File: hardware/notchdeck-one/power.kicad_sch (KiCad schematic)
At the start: 21 parts, among them J1 USB-C, J2 BAT 1S, Q1 AO3401A, U2 AP2112K-3.3, U3 MCP73831-2-OT, U4 MAX17048, U7 USBLC6-2SC6, U8 74LVC1G125

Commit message: Add schematic wiring notes support
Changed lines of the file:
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@@
 		(instances
 			(project "notchdeck-one"
-				(path "/9b1c0f7a-1d2e-4a3b-8c5d-0e6f7a8b9c01/7d2dd40e-5097-4a0f-9306-a516a342b95f"
+				(path "/9b1c0f7a-1d2e-4a3b-8c5d-0e6f7a8b9c01/2c77e6d8-3afb-4a5f-bda1-2cf5540b755c"
 					(reference "J1")
 					(unit 1)
@@
 		(instances
 			(project "notchdeck-one"
-				(path "/9b1c0f7a-1d2e-4a3b-8c5d-0e6f7a8b9c01/7d2dd40e-5097-4a0f-9306-a516a342b95f"
+				(path "/9b1c0f7a-1d2e-4a3b-8c5d-0e6f7a8b9c01/2c77e6d8-3afb-4a5f-bda1-2cf5540b755c"
 					(reference "U7")
 					(unit 1)
@@
 		(instances
 			(project "notchdeck-one"
-				(path "/9b1c0f7a-1d2e-4a3b-8c5d-0e6f7a8b9c01/7d2dd40e-5097-4a0f-9306-a516a342b95f"
+				(path "/9b1c0f7a-1d2e-4a3b-8c5d-0e6f7a8b9c01/2c77e6d8-3afb-4a5f-bda1-2cf5540b755c"
 					(reference "R1")
 					(unit 1)
@@
 		(instances
 			(project "notchdeck-one"
-				(path "/9b1c0f7a-1d2e-4a3b-8c5d-0e6f7a8b9c01/7d2dd40e-5097-4a0f-9306-a516a342b95f"
+				(path "/9b1c0f7a-1d2e-4a3b-8c5d-0e6f7a8b9c01/2c77e6d8-3afb-4a5f-bda1-2cf5540b755c"
 					(reference "R2")
 					(unit 1)
@@
 		(instances
 			(project "notchdeck-one"
-				(path "/9b1c0f7a-1d2e-4a3b-8c5d-0e6f7a8b9c01/7d2dd40e-5097-4a0f-9306-a516a342b95f"
+				(path "/9b1c0f7a-1d2e-4a3b-8c5d-0e6f7a8b9c01/2c77e6d8-3afb-4a5f-bda1-2cf5540b755c"
 					(reference "U3")
 					(unit 1)
@@
 		(instances
 			(project "notchdeck-one"
-				(path "/9b1c0f7a-1d2e-4a3b-8c5d-0e6f7a8b9c01/7d2dd40e-5097-4a0f-9306-a516a342b95f"
+				(path "/9b1c0f7a-1d2e-4a3b-8c5d-0e6f7a8b9c01/2c77e6d8-3afb-4a5f-bda1-2cf5540b755c"
 					(reference "R3")
 					(unit 1)
@@
 		(instances
 			(project "notchdeck-one"
-				(path "/9b1c0f7a-1d2e-4a3b-8c5d-0e6f7a8b9c01/7d2dd40e-5097-4a0f-9306-a516a342b95f"
+				(path "/9b1c0f7a-1d2e-4a3b-8c5d-0e6f7a8b9c01/2c77e6d8-3afb-4a5f-bda1-2cf5540b755c"
 					(reference "U2")
 					(unit 1)
@@
 		(instances
 			(project "notchdeck-one"
-				(path "/9b1c0f7a-1d2e-4a3b-8c5d-0e6f7a8b9c01/7d2dd40e-5097-4a0f-9306-a516a342b95f"
+				(path "/9b1c0f7a-1d2e-4a3b-8c5d-0e6f7a8b9c01/2c77e6d8-3afb-4a5f-bda1-2cf5540b755c"
 					(reference "C7")
 					(unit 1)
@@
 		(instances
 			(project "notchdeck-one"
-				(path "/9b1c0f7a-1d2e-4a3b-8c5d-0e6f7a8b9c01/7d2dd40e-5097-4a0f-9306-a516a342b95f"
+				(path "/9b1c0f7a-1d2e-4a3b-8c5d-0e6f7a8b9c01/2c77e6d8-3afb-4a5f-bda1-2cf5540b755c"
 					(reference "C8")
 					(unit 1)
@@
 		(instances
 			(project "notchdeck-one"
-				(path "/9b1c0f7a-1d2e-4a3b-8c5d-0e6f7a8b9c01/7d2dd40e-5097-4a0f-9306-a516a342b95f"
+				(path "/9b1c0f7a-1d2e-4a3b-8c5d-0e6f7a8b9c01/2c77e6d8-3afb-4a5f-bda1-2cf5540b755c"
 					(reference "C9")
 					(unit 1)
@@
 		(instances
 			(project "notchdeck-one"
-				(path "/9b1c0f7a-1d2e-4a3b-8c5d-0e6f7a8b9c01/7d2dd40e-5097-4a0f-9306-a516a342b95f"
+				(path "/9b1c0f7a-1d2e-4a3b-8c5d-0e6f7a8b9c01/2c77e6d8-3afb-4a5f-bda1-2cf5540b755c"
 					(reference "Q1")
 					(unit 1)
@@
 		(instances
 			(project "notchdeck-one"
-				(path "/9b1c0f7a-1d2e-4a3b-8c5d-0e6f7a8b9c01/7d2dd40e-5097-4a0f-9306-a516a342b95f"
+				(path "/9b1c0f7a-1d2e-4a3b-8c5d-0e6f7a8b9c01/2c77e6d8-3afb-4a5f-bda1-2cf5540b755c"
 					(reference "D_PP")
 					(unit 1)
@@
 		(instances
 			(project "notchdeck-one"
-				(path "/9b1c0f7a-1d2e-4a3b-8c5d-0e6f7a8b9c01/7d2dd40e-5097-4a0f-9306-a516a342b95f"
+				(path "/9b1c0f7a-1d2e-4a3b-8c5d-0e6f7a8b9c01/2c77e6d8-3afb-4a5f-bda1-2cf5540b755c"
 					(reference "R4")
 					(unit 1)
@@
 		(instances
 			(project "notchdeck-one"
-				(path "/9b1c0f7a-1d2e-4a3b-8c5d-0e6f7a8b9c01/7d2dd40e-5097-4a0f-9306-a516a342b95f"
+				(path "/9b1c0f7a-1d2e-4a3b-8c5d-0e6f7a8b9c01/2c77e6d8-3afb-4a5f-bda1-2cf5540b755c"
 					(reference "R5")
 					(unit 1)
@@
 		(instances
 			(project "notchdeck-one"
-				(path "/9b1c0f7a-1d2e-4a3b-8c5d-0e6f7a8b9c01/7d2dd40e-5097-4a0f-9306-a516a342b95f"
+				(path "/9b1c0f7a-1d2e-4a3b-8c5d-0e6f7a8b9c01/2c77e6d8-3afb-4a5f-bda1-2cf5540b755c"
 					(reference "U4")
 					(unit 1)
@@
 		(instances
 			(project "notchdeck-one"
-				(path "/9b1c0f7a-1d2e-4a3b-8c5d-0e6f7a8b9c01/7d2dd40e-5097-4a0f-9306-a516a342b95f"
+				(path "/9b1c0f7a-1d2e-4a3b-8c5d-0e6f7a8b9c01/2c77e6d8-3afb-4a5f-bda1-2cf5540b755c"
 					(reference "C10")
 					(unit 1)
@@
 		(instances
 			(project "notchdeck-one"
-				(path "/9b1c0f7a-1d2e-4a3b-8c5d-0e6f7a8b9c01/7d2dd40e-5097-4a0f-9306-a516a342b95f"
+				(path "/9b1c0f7a-1d2e-4a3b-8c5d-0e6f7a8b9c01/2c77e6d8-3afb-4a5f-bda1-2cf5540b755c"
 					(reference "R6")
 					(unit 1)
@@
 		(instances
 			(project "notchdeck-one"
-				(path "/9b1c0f7a-1d2e-4a3b-8c5d-0e6f7a8b9c01/7d2dd40e-5097-4a0f-9306-a516a342b95f"
+				(path "/9b1c0f7a-1d2e-4a3b-8c5d-0e6f7a8b9c01/2c77e6d8-3afb-4a5f-bda1-2cf5540b755c"
 					(reference "R7")
 					(unit 1)
@@
 		(instances
 			(project "notchdeck-one"
-				(path "/9b1c0f7a-1d2e-4a3b-8c5d-0e6f7a8b9c01/7d2dd40e-5097-4a0f-9306-a516a342b95f"
+				(path "/9b1c0f7a-1d2e-4a3b-8c5d-0e6f7a8b9c01/2c77e6d8-3afb-4a5f-bda1-2cf5540b755c"
 					(reference "R8")
 					(unit 1)
@@
 		(instances
 			(project "notchdeck-one"
-				(path "/9b1c0f7a-1d2e-4a3b-8c5d-0e6f7a8b9c01/7d2dd40e-5097-4a0f-9306-a516a342b95f"
+				(path "/9b1c0f7a-1d2e-4a3b-8c5d-0e6f7a8b9c01/2c77e6d8-3afb-4a5f-bda1-2cf5540b755c"
 					(reference "J2")
 					(unit 1)
@@
 		(instances
 			(project "notchdeck-one"
-				(path "/9b1c0f7a-1d2e-4a3b-8c5d-0e6f7a8b9c01/7d2dd40e-5097-4a0f-9306-a516a342b95f"
+				(path "/9b1c0f7a-1d2e-4a3b-8c5d-0e6f7a8b9c01/2c77e6d8-3afb-4a5f-bda1-2cf5540b755c"
 					(reference "U8")
 					(unit 1)
@@
 		(exclude_from_sim no)
 		(at 15.00 175.00 0)
-		(effects (font (size 1.5 1.5)) (justify left top))
+		(effects (font (face "Courier New") (size 1.27 1.27)) (justify left top))
 	)
 	(sheet_instances

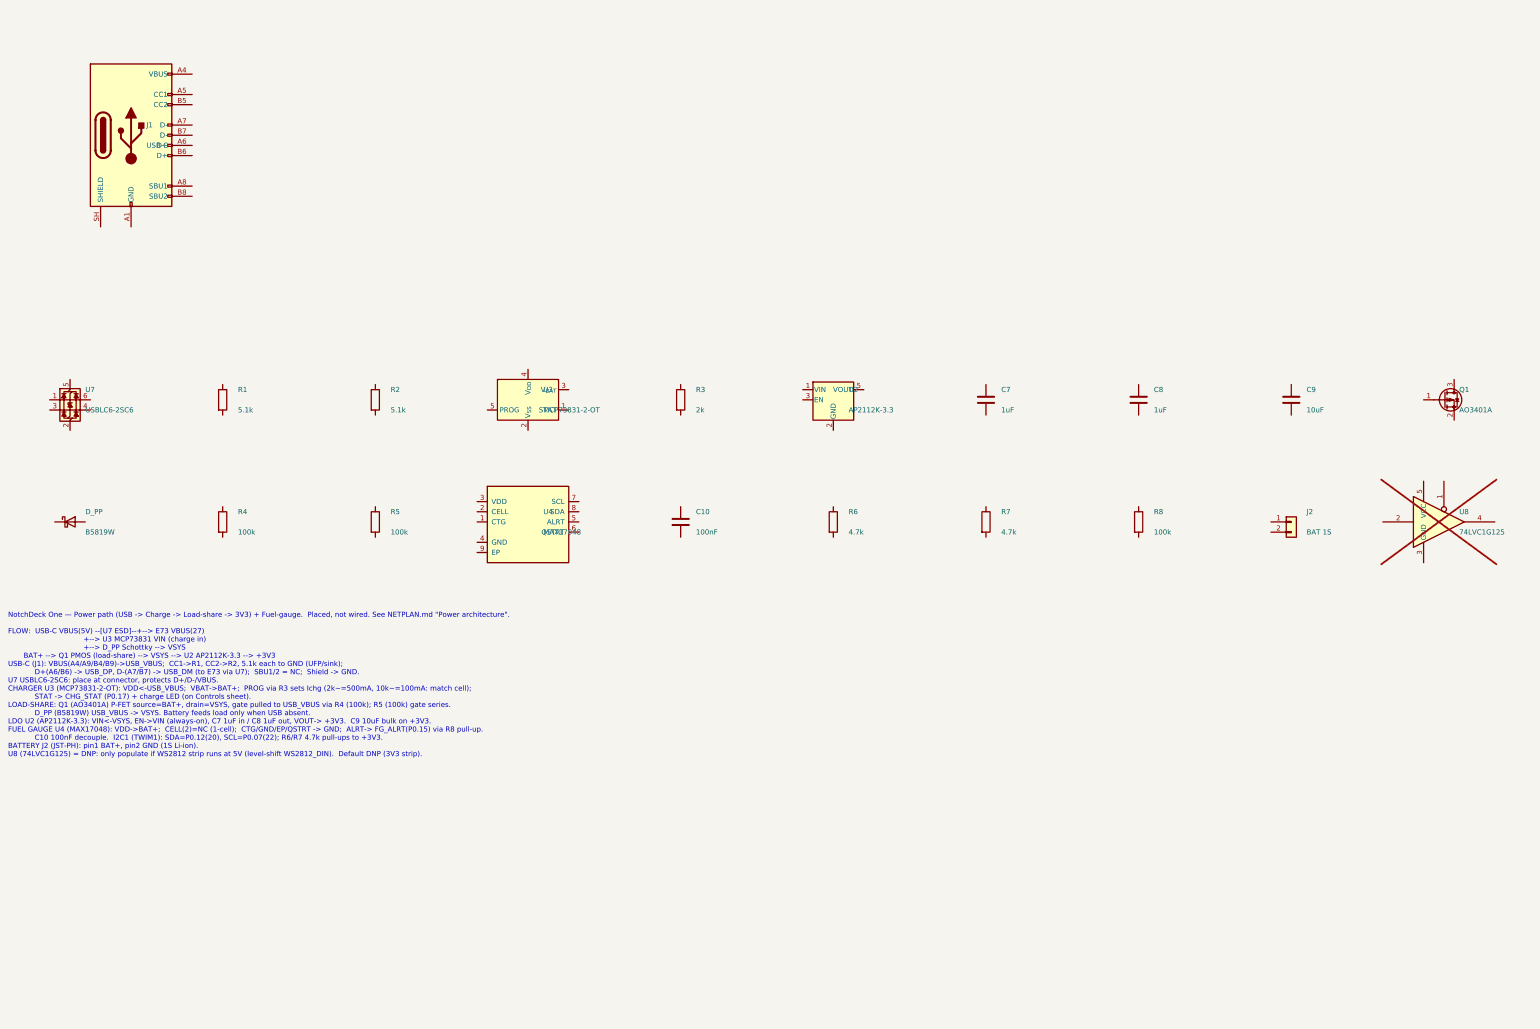
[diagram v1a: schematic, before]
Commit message: Wire and verify NotchDeck controller schematics
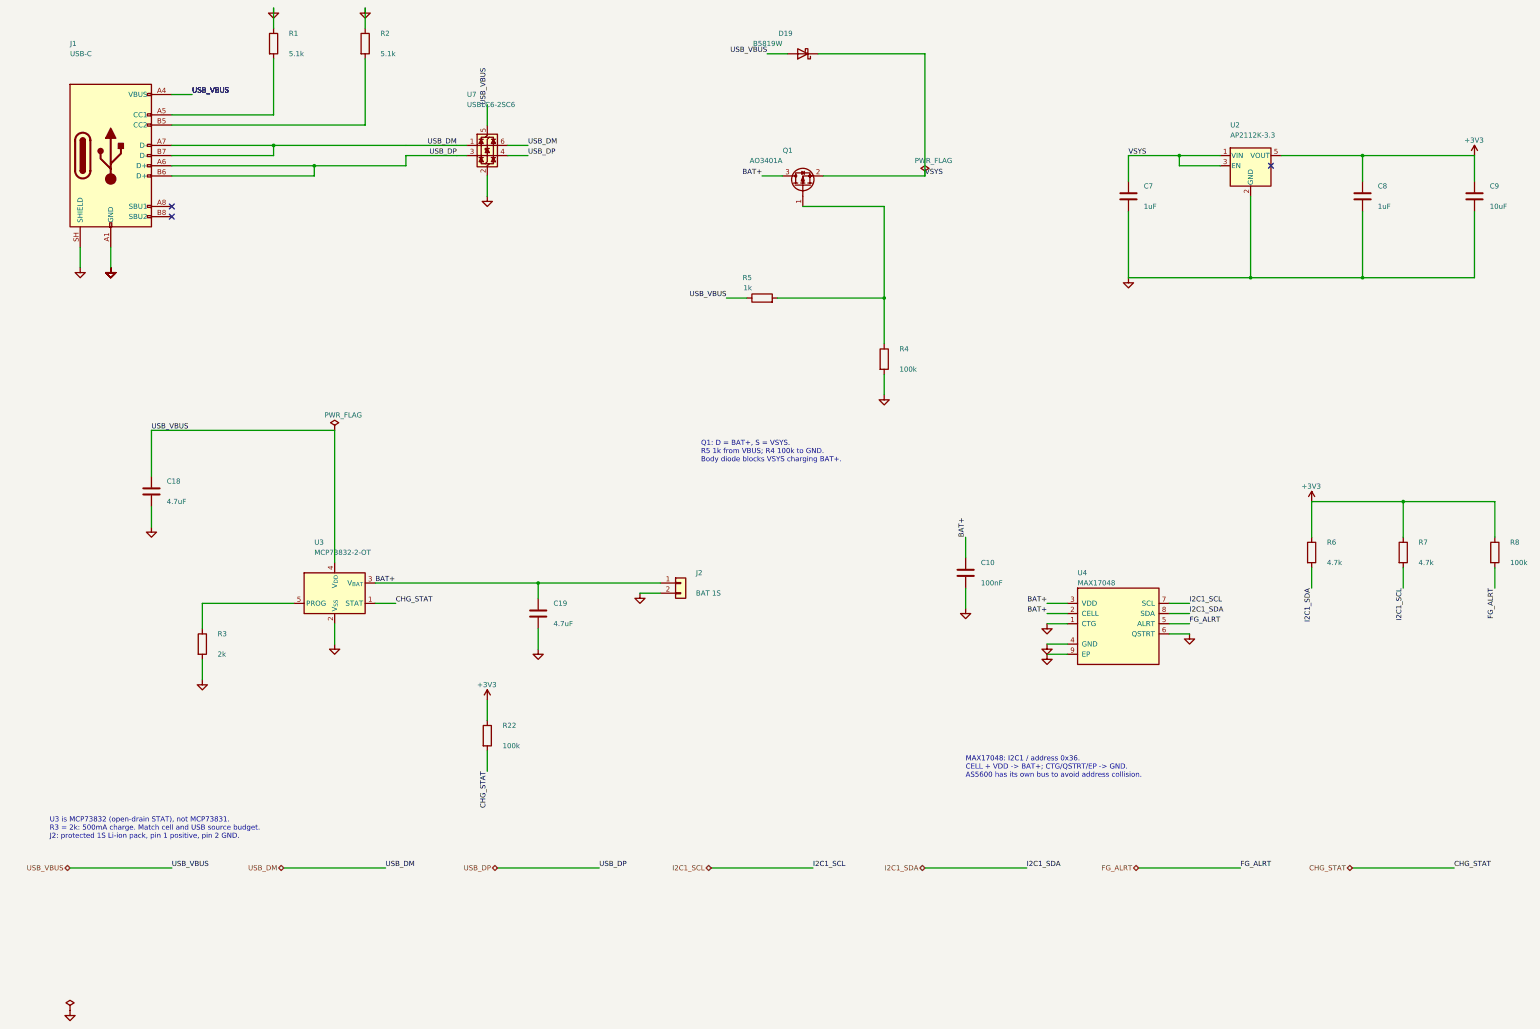
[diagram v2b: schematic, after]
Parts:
- removed D_PP: B5819W, Diode_SMD:D_SOD-123, symbol Device:D_Schottky
- removed U3: MCP73831-2-OT, Package_TO_SOT_SMD:SOT-23-5, symbol Battery_Management:MCP73831-2-OT
- removed U8: 74LVC1G125, Package_TO_SOT_SMD:SOT-23-5, symbol 74xGxx:74LVC1G125
- added C18, C19: 4.7uF, Capacitor_SMD:C_0805_2012Metric, symbol Device:C
- added D19: B5819W, Diode_SMD:D_SOD-123, symbol Device:D_Schottky
- added R22: 100k, Resistor_SMD:R_0402_1005Metric, symbol Device:R
- added U3: MCP73832-2-OT, Package_TO_SOT_SMD:SOT-23-5, symbol Battery_Management:MCP73832-2-OT
- R5: value 100k -> 1k
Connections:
- net at R3.1: now also U3.5 (PROG)
- net GND: now reaches R3.2
- net GND: now also C10.2, C7.2, C8.2, C9.2, J1.A1 (GND), J1.A12 (GND), J1.B1 (GND), J1.B12 (GND), J1.SH (SHIELD), J2.2 (Pin_2), R1.1, R2.1, R4.2, U2.2 (GND), U4.1 (CTG), U4.4 (GND), U4.6 (QSTRT), U4.9 (EP), U7.2 (GND), C18.2, C19.2, U3.2 (V_{SS})
- net +3V3: now reaches R8.1
- net +3V3: now also C8.1, C9.1, R6.1, R7.1, U2.5 (VOUT), R22.1
- net FG_ALRT: now reaches R8.2
- net FG_ALRT: now also U4.5 (ALRT)
- net at Q1.1 (G): now also R4.1, R5.2
- net VSYS: now reaches Q1.2 (S)
- net VSYS: now also C7.1, U2.1 (VIN), U2.3 (EN), D19.1 (K)
- net BAT+: now reaches Q1.3 (D)
- net BAT+: now also C10.1, J2.1 (Pin_1), U4.2 (CELL), U4.3 (VDD), C19.1, U3.3 (V_{BAT})
- net at R1.2: now also J1.A5 (CC1)
- net I2C1_SDA: now reaches R6.2
- net I2C1_SDA: now also U4.8 (SDA)
- net I2C1_SCL: now reaches U4.7 (SCL)
- net I2C1_SCL: now also R7.2
- net USB_VBUS: now reaches J1.A4 (VBUS), J1.A9 (VBUS), J1.B4 (VBUS), J1.B9 (VBUS)
- net USB_VBUS: now also R5.1, U7.5 (VBUS), C18.1, D19.2 (A), U3.4 (V_{DD})
- net USB_DP: now reaches J1.A6 (D+)
- net USB_DP: now also J1.B6 (D+), U7.3 (I/O2), U7.4 (I/O2)
- net USB_DM: now reaches J1.A7 (D-)
- net USB_DM: now also J1.B7 (D-), U7.1 (I/O1), U7.6 (I/O1)
- net at J1.B5 (CC2): now also R2.2
- new net CHG_STAT: R22.2, U3.1 (STAT)
- no-connect marks 0 -> 3
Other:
- note added: "MAX17048: I2C1 / address 0x36. CELL + VDD -> BAT+; CTG/QSTRT/EP -> GND. AS5600 has its own bus to avoid address collision."
- note added: "Q1: D = BAT+, S = VSYS. R5 1k from VBUS; R4 100k to GND. Body diode blocks VSYS charging BAT+."
- note added: "U3 is MCP73832 (open-drain STAT), not MCP73831. R3 = 2k: 500mA charge. Match cell and USB source budget. J2: protected 1S Li-ion pack, pin 1 positive, pin 2 GND."
- note removed: "NotchDeck One — Power path (USB -> Charge -> Load-share -> 3V3) + Fuel-gauge. Placed, not wired. See NETPLAN.md "Power architecture". FLOW: USB-C VBUS(5V) --[U7 ESD]--+--> E73 VBUS(27) +--> U3 MCP73831 VIN (charge in) +--> D_PP Schottky --> VSYS BAT+ --> Q1 PMOS (load-share) --> VSYS --> U2 AP2112K-3.3 --> +3V3 USB-C (J1): VBUS(A4/A9/B4/B9)->USB_VBUS; CC1->R1, CC2->R2, 5.1k each to GND (UFP/sink)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"
- title: NotchDeck One — Power (USB-C / Charge / LDO / Fuel-gauge) -> NotchDeck One — Power and battery

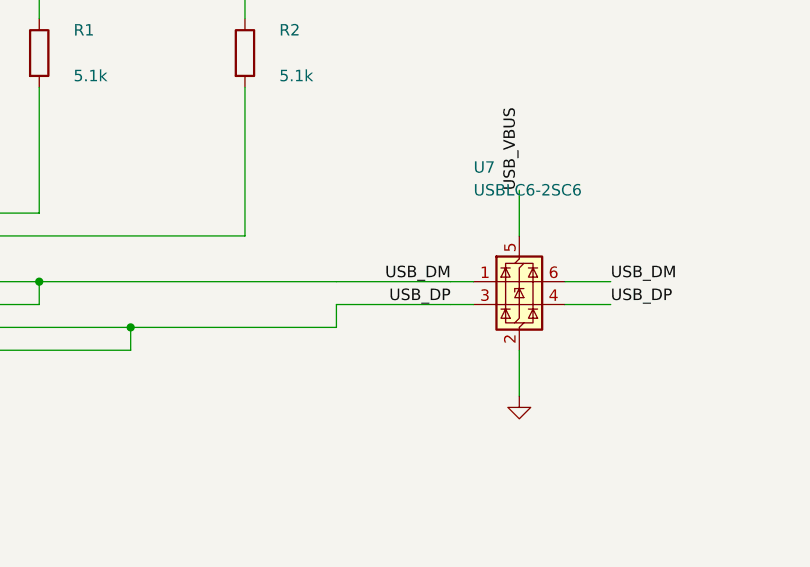
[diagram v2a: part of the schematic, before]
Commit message: Add verified provisional controller PCB floorplan
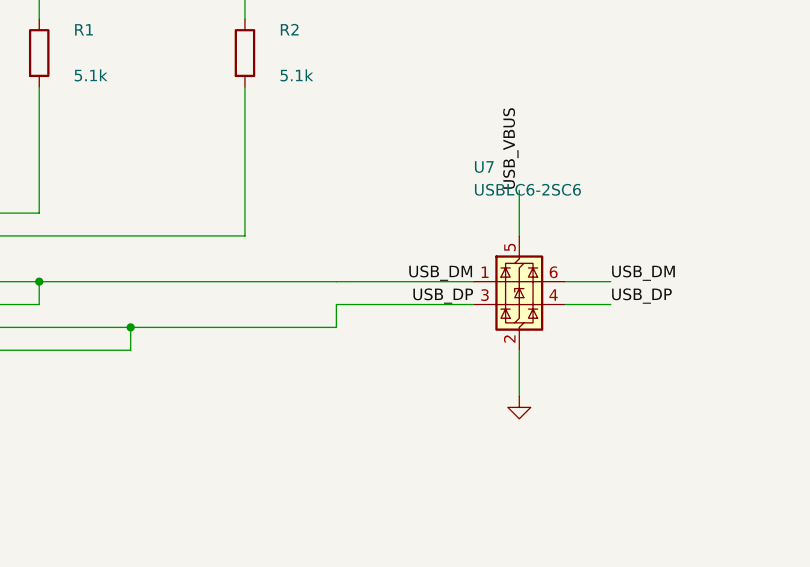
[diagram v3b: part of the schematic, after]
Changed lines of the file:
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@@
 		(stroke (width 0) (type default))
 	)
-	(wire (pts (xy 114.3000 58.4200) (xy 127.0000 58.4200))
+	(wire (pts (xy 114.3000 58.4200) (xy 129.5400 58.4200))
 		(stroke (width 0) (type default))
 	)
@@
 		(stroke (width 0) (type default))
 	)
-	(wire (pts (xy 114.3000 60.9600) (xy 127.0000 60.9600))
-		(stroke (width 0) (type default))
-	)
-	(wire (pts (xy 127.0000 58.4200) (xy 129.5400 58.4200))
-		(stroke (width 0) (type default))
-	)
-	(wire (pts (xy 127.0000 60.9600) (xy 129.5400 60.9600))
+	(wire (pts (xy 114.3000 60.9600) (xy 129.5400 60.9600))
 		(stroke (width 0) (type default))
 	)
@@
 	(no_connect (at 55.88 76.2))
 	(label "USB_DM"
-		(at 127.0000 58.4200 180)
+		(at 129.5400 58.4200 180)
 		(effects (font (size 1.27 1.27)) (justify right bottom))
 	)
@@
 	)
 	(label "USB_DP"
-		(at 127.0000 60.9600 180)
+		(at 129.5400 60.9600 180)
 		(effects (font (size 1.27 1.27)) (justify right bottom))
 	)

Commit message: Source controller BOM from JLCPCB and align selected footprints
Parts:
- C10: BOM Checked (none) -> 2026-10-03; BOM Comments (none) -> 100nF 16V X7R ±10% 0402 Multilayer Ceramic Capacitors MLCC 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; JLCPCB Part Type (none) -> Basic; LCSC (none) -> C1525; MPN (none) -> CL05B104KO5NNNC; Manufacturer (none) -> Samsung Electro-Mechanics
- C18, C19: BOM Checked (none) -> 2026-10-03; BOM Comments (none) -> 25V 4.7uF X5R ±10% 0805 Multilayer Ceramic Capacitors MLCC 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; JLCPCB Part Type (none) -> Basic; LCSC (none) -> C1779; MPN (none) -> CL21A475KAQNNNE; Manufacturer (none) -> Samsung Electro-Mechanics
- C7, C8: BOM Checked (none) -> 2026-10-03; BOM Comments (none) -> 1uF 25V X5R ±10% 0402 Multilayer Ceramic Capacitors MLCC - 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; JLCPCB Part Type (none) -> Basic; LCSC (none) -> C52923; MPN (none) -> CL05A105KA5NQNC; Manufacturer (none) -> Samsung Electro-Mechanics
- C9: BOM Checked (none) -> 2026-10-03; BOM Comments (none) -> 10uF 25V X5R ±10% 0805 Multilayer Ceramic Capacitors MLCC -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; JLCPCB Part Type (none) -> Basic; LCSC (none) -> C15850; MPN (none) -> CL21A106KAYNNNE; Manufacturer (none) -> Samsung Electro-Mechanics
- D19: BOM Checked (none) -> 2026-10-03; JLCPCB Part Type (none) -> Basic; MPN B5819W -> B5819W SL; Manufacturer Slkor -> JSCJ
- J1: BOM Checked (none) -> 2026-10-03; JLCPCB Part Type (none) -> Extended; Manufacturer (none) -> Korean Hroparts Elec
- J2: BOM Checked (none) -> 2026-10-03; BOM Comments (none) -> Mating harnesses not included. J2: protected 1S cell, pin 1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; JLCPCB Part Type (none) -> Extended; LCSC (none) -> C295747; MPN S2B-PH-SM4-TB -> S2B-PH-SM4-TB(LF)(SN)
- Q1: BOM Checked (none) -> 2026-10-03; JLCPCB Part Type (none) -> Basic
- R1, R2: BOM Checked (none) -> 2026-10-03; BOM Comments (none) -> -55℃~+155℃ 5.1kΩ 50V 62.5mW Thick Film Resistor ±1% ±100ppm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; JLCPCB Part Type (none) -> Basic; LCSC (none) -> C25905; MPN (none) -> 0402WGF5101TCE; Manufacturer (none) -> UNI-ROYAL
- R22, R4, R8: BOM Checked (none) -> 2026-10-03; BOM Comments (none) -> -55℃~+155℃ 100kΩ 50V 62.5mW Thick Film Resistor ±1% ±100ppm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; JLCPCB Part Type (none) -> Basic; LCSC (none) -> C25741; MPN (none) -> 0402WGF1003TCE; Manufacturer (none) -> UNI-ROYAL
- R3: BOM Checked (none) -> 2026-10-03; BOM Comments (none) -> -55℃~+155℃ 2kΩ 50V 62.5mW Thick Film Resistor ±1% ±100ppm/℃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; JLCPCB Part Type (none) -> Basic; LCSC (none) -> C4109; MPN (none) -> 0402WGF2001TCE; Manufacturer (none) -> UNI-ROYAL
- R5: BOM Checked (none) -> 2026-10-03; BOM Comments (none) -> -55℃~+155℃ 1kΩ 50V 62.5mW Thick Film Resistor ±1% ±100ppm/℃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; JLCPCB Part Type (none) -> Basic; LCSC (none) -> C11702; MPN (none) -> 0402WGF1001TCE; Manufacturer (none) -> UNI-ROYAL
- R6, R7: BOM Checked (none) -> 2026-10-03; BOM Comments (none) -> -55℃~+155℃ 4.7kΩ 50V 62.5mW Thick Film Resistor ±1% ±100ppm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; JLCPCB Part Type (none) -> Basic; LCSC (none) -> C25900; MPN (none) -> 0402WGF4701TCE; Manufacturer (none) -> UNI-ROYAL
- U2: BOM Checked (none) -> 2026-10-03; JLCPCB Part Type (none) -> Extended; LCSC C23380830 -> C51118; Manufacturer Diodes -> DIODES
- U3: BOM Checked (none) -> 2026-10-03; BOM Comments (none) -> MCP73832 open-drain STAT required; do not substitute MCP738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; JLCPCB Part Type (none) -> Extended; LCSC (none) -> C38066; Manufacturer Microchip -> MICROCHIP
- U4: BOM Checked (none) -> 2026-10-03; BOM Comments (none) -> Exact MAX17048G+T10 TDFN variant; land-pattern review remai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; JLCPCB Part Type (none) -> Extended; Manufacturer Analog Devices -> MAXIM
- U7: BOM Checked (none) -> 2026-10-03; JLCPCB Part Type (none) -> Extended; LCSC C2687116 -> C7519
